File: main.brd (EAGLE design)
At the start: 23.6 x 22.9 mm, 23 parts, among them Q1 BSS84, U1 433MHz, U2 ATMEGA328P-MU-QFN32

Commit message: Started redesign
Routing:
- net +3V3: track 44.6 -> 47.6 mm
- net !SBUS: track 34.6 -> 37.6 mm
- net N$2: track 25.9 -> 28.4 mm
- net N$6: track 34.3 -> 36.3 mm
- net MISO: track 22.6 -> 24.3 mm
- net SCK: track 22.5 -> 21.1 mm
- net +5V: track 52.8 -> 51.8 mm
- net PPM1: track 19.2 -> 18.6 mm

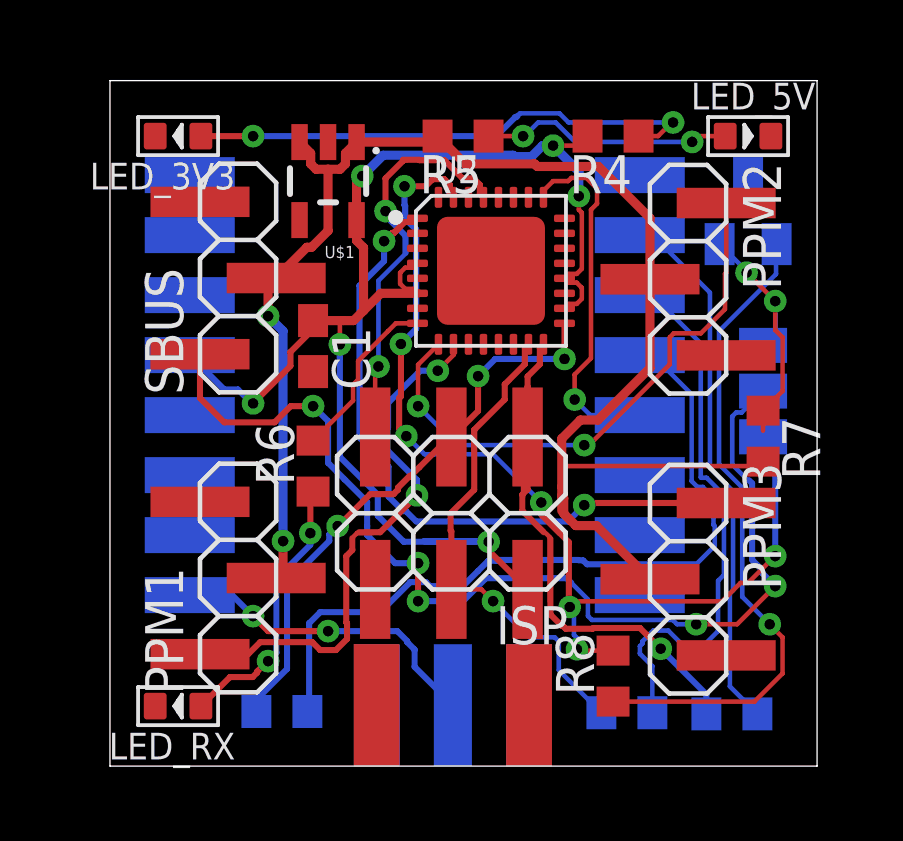
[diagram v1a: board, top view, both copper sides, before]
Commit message: Adapted to the new design rules
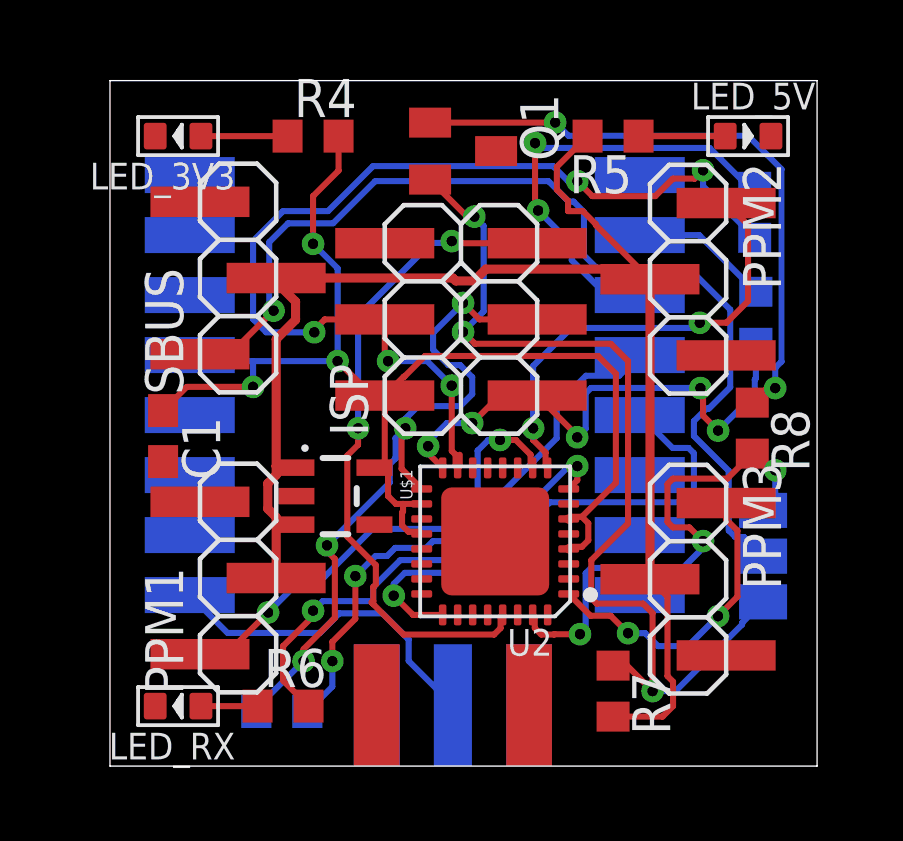
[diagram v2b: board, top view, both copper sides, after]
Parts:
- moved R2 17.2 mm to (20.2, 19.5), turned to 90 degrees
- moved R3 13.2 mm to (20.3, 16.0), turned to 90 degrees
- moved U$1 10.5 mm to (6.25, 10.0), turned to 270 degrees
- moved R4 10.0 mm to (5.50, 22.0), turned to 0 degrees
- moved R7 9.86 mm to (15.5, 3.50)
- moved Q1 9.71 mm to (10.5, 21.5), flipped to the top, turned to 270 degrees
- moved R8 9.48 mm to (20.1, 12.3), turned to 270 degrees
- moved U2 9.02 mm to (11.6, 8.49), turned to 180 degrees
- moved R6 8.06 mm to (4.50, 3.00), turned to 0 degrees
- moved ISP 6.83 mm to (9.16, 14.6), turned to 90 degrees
- moved C1 5.83 mm to (0.50, 12.0)
- moved SJ1 5.50 mm to (20.5, 8.00), turned to 90 degrees
- moved R5 5.00 mm to (15.5, 22.0)
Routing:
- net SBUS: track 9.01 -> 32.0 mm, vias 2 -> 3
- net !SBUS: track 37.6 -> 17.1 mm, vias 7 -> 3
- net MOSI: track 17.8 -> 34.4 mm, vias 1 -> 5
- net N$7: track 17.5 -> 2.89 mm, vias 2 -> 0
- net N$4: track 18.2 -> 4.65 mm
- net PPM3: track 23.2 -> 10.3 mm
- net STATUS: track 5.77 -> 15.9 mm, vias 0 -> 2
- net N$2: track 28.4 -> 18.4 mm, vias 0 -> 2
- net !RESET: track 13.7 -> 22.6 mm
- net N$5: track 9.15 -> 1.89 mm, vias 2 -> 0
- net MISO: track 24.3 -> 17.9 mm, vias 1 -> 5
- net N$8: track 8.42 -> 2.89 mm, vias 2 -> 0
- net +3V3: track 47.6 -> 42.1 mm, vias 6 -> 3
- net !SS: track 12.1 -> 17.3 mm
- net PPM2: track 19.1 -> 15.2 mm
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
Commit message: Moved SMA Connector
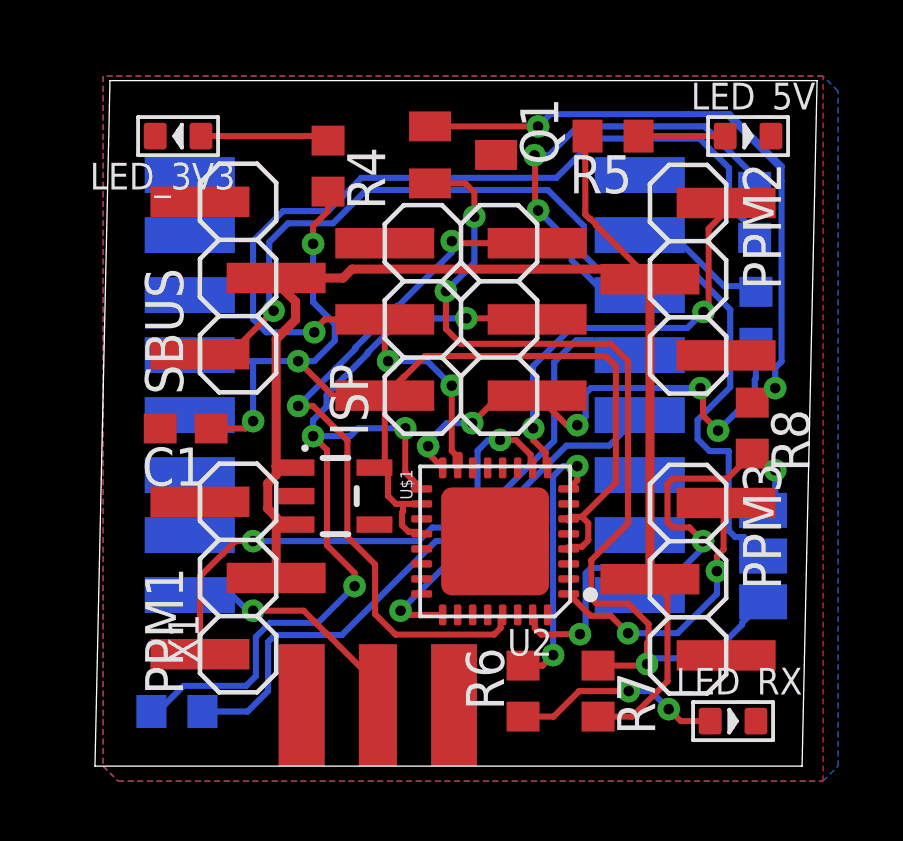
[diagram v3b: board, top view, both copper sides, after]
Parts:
- moved LED_RX 18.5 mm to (19.5, 2.50), turned to 0 degrees
- moved R6 8.02 mm to (12.5, 3.50), turned to 90 degrees
- moved R1 3.50 mm to (0.96, 2.82)
- moved X1 2.50 mm to (7.66, 1.00), flipped to the top
- moved R4 1.12 mm to (6.00, 21.0), turned to 270 degrees
- moved C1 0.80 mm to (1.25, 12.3), turned to 180 degrees
- moved R7 0.50 mm to (15.0, 3.50)
- moved Q1 0.13 mm to (10.5, 21.4)
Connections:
- removed net GND1: X1.GND@4
- removed net GND2: X1.GND@3
- removed net GND3: X1.GND@2
- removed net GND4: X1.GND@1
- net GND: now also X1.GND@1, X1.GND@2, X1.GND@3, X1.GND@4
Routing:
- net STATUS: track 15.9 -> 9.22 mm
- net SCK: track 23.9 -> 30.4 mm
- net !SS: track 17.3 -> 12.1 mm
- net N$5: track 1.89 -> 7.00 mm, vias 0 -> 2
- net N$2: track 18.4 -> 22.4 mm, vias 2 -> 0
- net N$10: track 20.7 -> 24.0 mm
- net N$1: track 11.2 -> 8.20 mm, vias 0 -> 1
- net PPM1: track 15.6 -> 17.1 mm
- net N$7: track 2.89 -> 4.30 mm
- net +5V: track 48.4 -> 47.0 mm
- net +3V3: track 42.1 -> 40.8 mm
- net PPM2: track 15.2 -> 14.0 mm
- net !RESET: track 22.6 -> 23.8 mm
- net PPM3: track 10.3 -> 9.18 mm
- net N$3: track 15.1 -> 15.8 mm
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- added copper zone on layer 1, net GND
- added copper zone on layer 16, net GND
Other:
- board size 23.6 x 22.9 mm -> 24.1 x 22.9 mm

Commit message: Starting fixing all DRC issues, only GND issues left
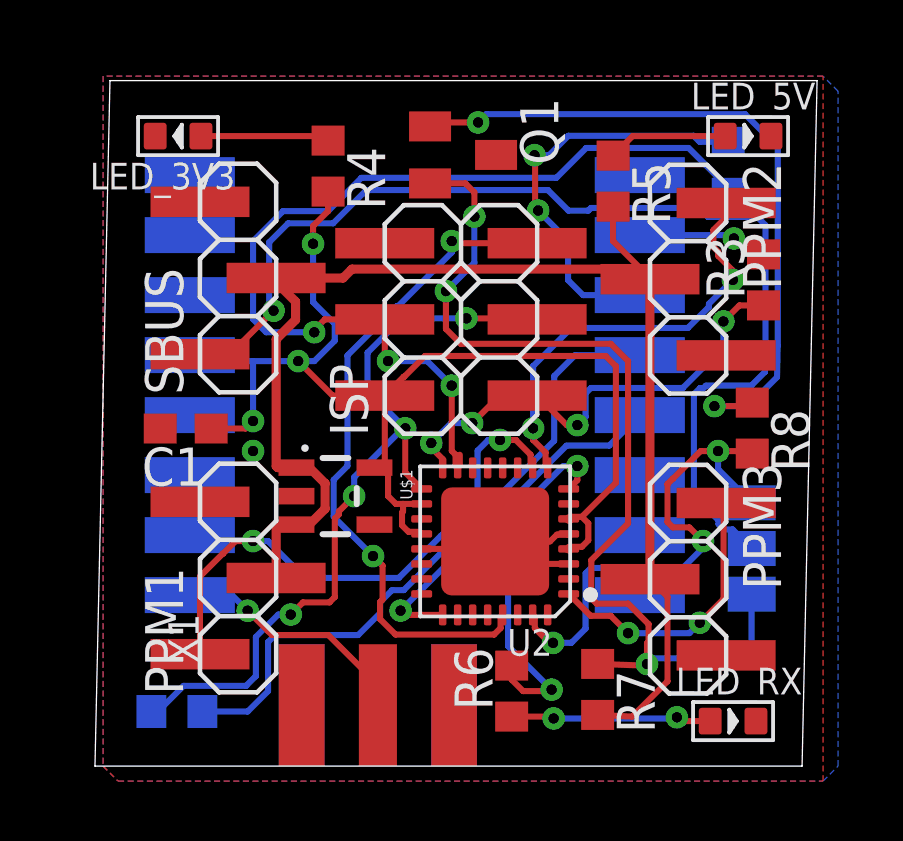
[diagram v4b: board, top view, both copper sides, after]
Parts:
- moved R2 1.74 mm to (19.3, 21.0)
- moved R5 1.50 mm to (15.5, 20.5), turned to 270 degrees
- moved R3 1.27 mm to (20.5, 17.2), flipped to the top
- moved SJ1 0.46 mm to (20.1, 8.25)
- moved R6 0.38 mm to (12.1, 3.50)
- moved R7 0.06 mm to (15.0, 3.56)
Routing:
- net GND: track 0.00 -> 6.49 mm
- net SCK: track 30.4 -> 27.0 mm
- net STATUS: track 9.22 -> 12.4 mm
- net N$6: track 33.8 -> 36.9 mm
- net MOSI: track 35.0 -> 32.4 mm
- net +5V: track 47.0 -> 45.2 mm
- net N$3: track 15.8 -> 14.0 mm
- net MISO: track 17.3 -> 15.7 mm, vias 5 -> 4
- net !RESET: track 23.8 -> 22.6 mm
- net N$8: track 2.89 -> 4.01 mm
- net PPM3: track 9.18 -> 10.3 mm
- net PPM2: track 14.0 -> 15.0 mm
- net PPM1: track 17.1 -> 18.1 mm
- net SBUS: track 31.5 -> 32.2 mm
- net N$4: track 4.65 -> 4.39 mm, vias 0 -> 1

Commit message: Changed some pins to simplify the layout
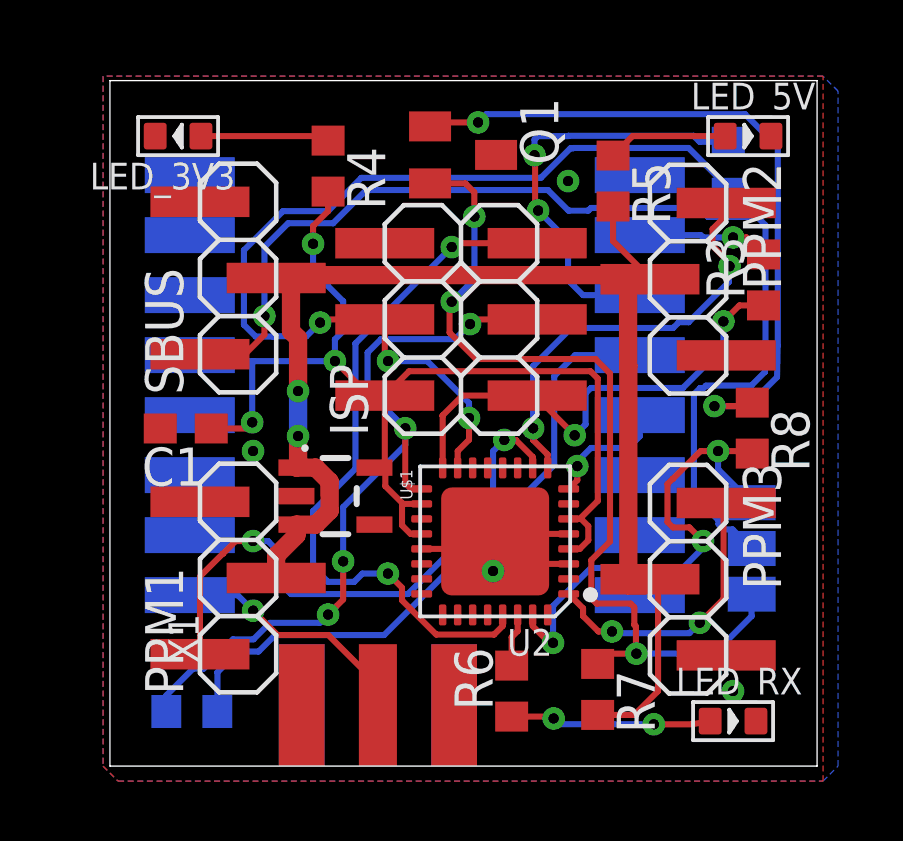
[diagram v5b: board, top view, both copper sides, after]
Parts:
- moved R1 0.50 mm to (1.46, 2.82)
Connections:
- net !SS: now also U2.8; no longer U2.25
- net STATUS: now also U2.30; no longer U2.8
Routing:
- net STATUS: track 12.4 -> 1.77 mm, vias 2 -> 0
- net !SS: track 12.1 -> 4.17 mm
- net SBUS: track 32.2 -> 29.9 mm
- net +5V: track 45.2 -> 47.2 mm, vias 0 -> 2
- net MISO: track 15.7 -> 17.5 mm, vias 4 -> 2
- net +3V3: track 40.8 -> 39.1 mm
- net GND: track 6.49 -> 7.98 mm, vias 0 -> 4
- net PPM1: track 18.1 -> 19.3 mm
- net !RESET: track 22.6 -> 23.7 mm
- net PPM2: track 15.0 -> 14.3 mm
- net SCK: track 27.0 -> 26.3 mm
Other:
- board size 24.1 x 22.9 mm -> 23.6 x 22.9 mm
